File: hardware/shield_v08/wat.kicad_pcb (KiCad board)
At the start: 2 copper layers, 37 parts, among them P101 24VOL, P102 CAUDAL_1, P103 V_IN, P104 PRESION_1, P105 INTENSIDAD_1, P106 18b20, P107 INTENSIDAD_2, P108 15VOL, P109 LCD_I2C, P110 ARD_DI_06, P111 ARD_ALI_04, P112 ARD_AN_04, P113 ARD_I2C_02, U101 ESP-12, U102 Recom-rd, U103 RO-1224S, U104 LM1117, U105 mp-1584

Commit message: [pcb]mejoras version 3
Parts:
- removed P113: ARD_I2C_02, Pin_Headers:Pin_Header_Straight_1x02
- added U106: NANO, oscar_libreria_huellas:arduino_nano, F.Cu at (203.3, 53.2)
- P112: value ARD_AN_04 -> ARD_AN_I2C_06
- moved D104 190.1 mm to (240.0, 27.5)
- moved F101 177.6 mm to (234.5, 24.0), turned to 270 degrees
- moved C109 174.6 mm to (231.7, 62.0), turned to 270 degrees
- moved P110 173.3 mm to (210.9, 45.6), turned to 270 degrees
- moved P103 171.9 mm to (247.0, 20.0), turned to 180 degrees
- moved U101 156.1 mm to (159.1, 32.1), turned to 90 degrees
- moved C108 149.7 mm to (169.0, 38.5)
- moved C105 147.9 mm to (247.5, 33.5)
- moved U105 147.6 mm to (244.0, 49.5), turned to 270 degrees
- moved P101 146.3 mm to (221.0, 95.5), turned to 0 degrees
- moved P108 137.6 mm to (234.0, 95.5), turned to 0 degrees
- moved C106 136.1 mm to (169.0, 45.0), turned to 0 degrees
- moved U103 128.8 mm to (224.5, 80.0), turned to 270 degrees
- moved C107 128.0 mm to (247.5, 64.5), turned to 270 degrees
- moved P102 124.6 mm to (207.5, 19.5), turned to 180 degrees
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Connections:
- P103 pad 1: Net-(F101-Pad1) -> GND
- P103 pad 2: GND -> Net-(F101-Pad1)
- P104 pad 1: GND -> Net-(C103-Pad1)
- P104 pad 2: Net-(C103-Pad1) -> GND
- P105 pad 1: GND -> Net-(C101-Pad1)
- P105 pad 2: Net-(C101-Pad1) -> GND
- P106 pad 1: /Vpc_5V -> GND
- P106 pad 3: GND -> /Vpc_5V
- P107 pad 1: GND -> Net-(C102-Pad1)
- P107 pad 2: Net-(C102-Pad1) -> GND
- P110 pad 3: /e_rx -> /18b20
- P110 pad 4: /e_tx -> /e_rx
- P110 pad 5: /e_rst -> /e_tx
- P110 pad 6: /18b20 -> /e_rst
- P112 pad 5: (no net) -> /sda
- P112 pad 6: (no net) -> /scl

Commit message: [pcb]repongo librerias de huellas
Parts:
- P112: value ARD_AN_I2C_06 -> ARD_AN_I2C
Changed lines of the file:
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@@
       (effects (font (size 1 1) (thickness 0.15)))
     )
-    (fp_text value ARD_AN_I2C_06 (at 0 -3.1 90) (layer F.Fab)
+    (fp_text value ARD_AN_I2C (at 0 -3.1 90) (layer F.Fab)
       (effects (font (size 1 1) (thickness 0.15)))
     )

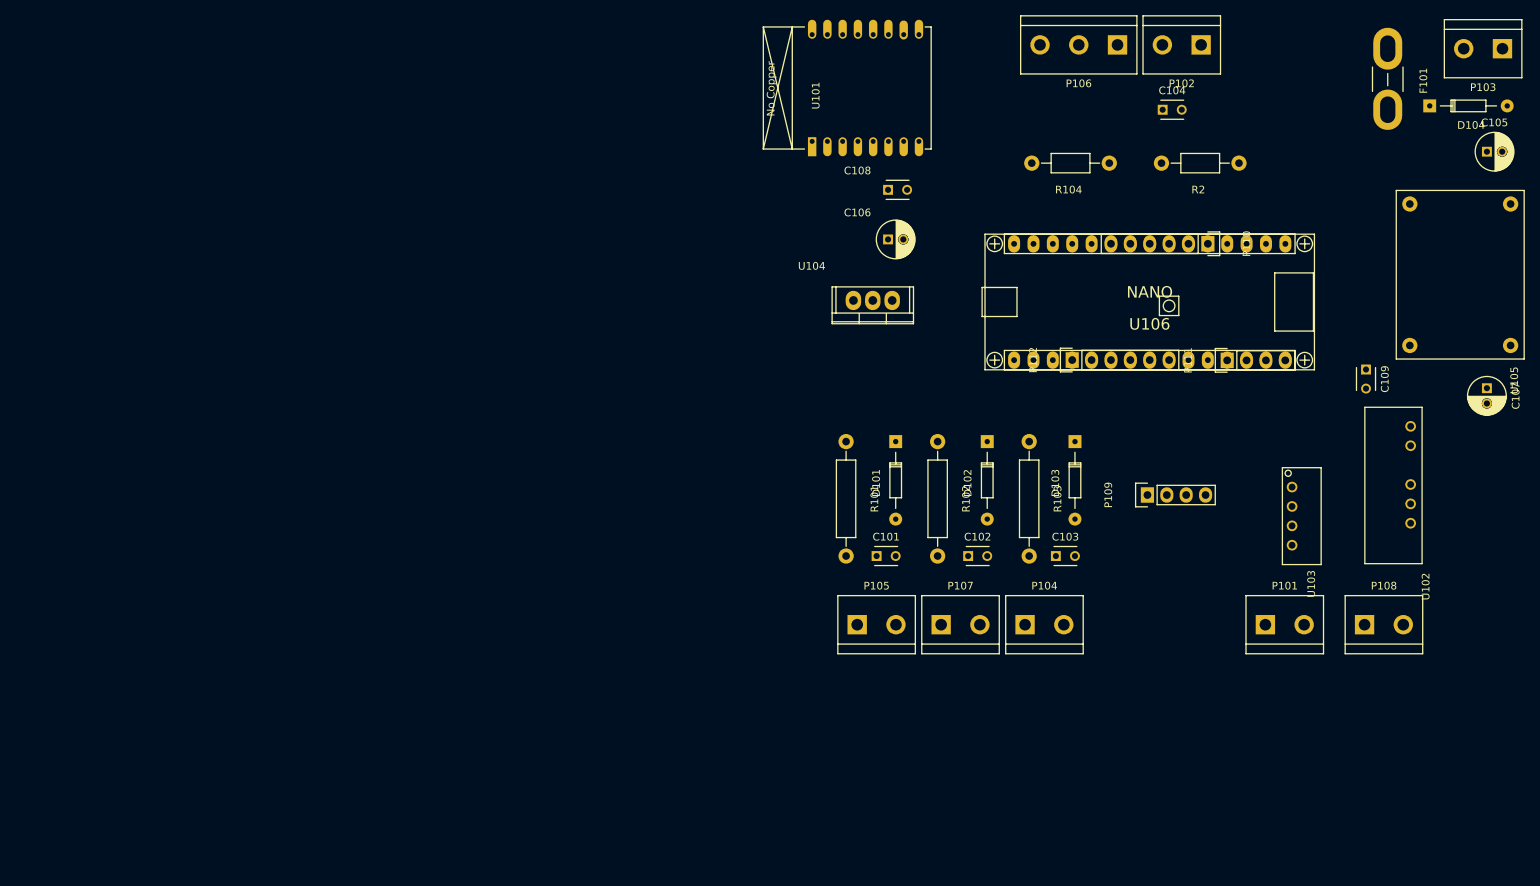
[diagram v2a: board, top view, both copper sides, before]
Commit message: [pdb] cambio posicion nano
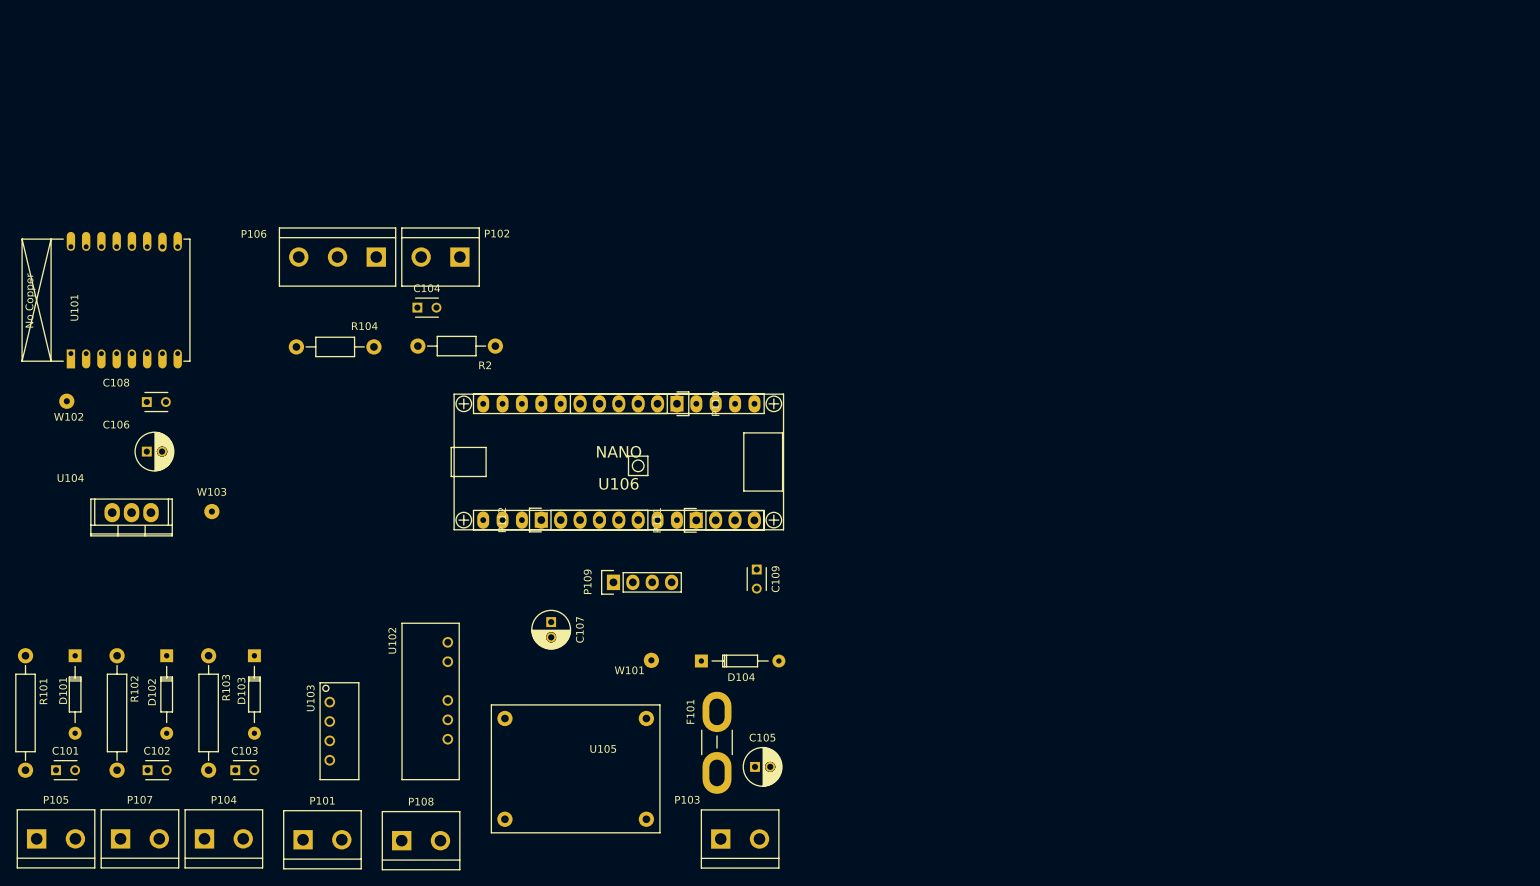
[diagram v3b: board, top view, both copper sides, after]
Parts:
- added W101: +12V, Wire_Pads:SolderWirePad_single_0-8mmDrill, F.Cu at (138.0, 100.2)
- added W102: +3,3V, Wire_Pads:SolderWirePad_single_0-8mmDrill, F.Cu at (61.4, 66.2)
- added W103: +8V, Wire_Pads:SolderWirePad_single_0-8mmDrill, F.Cu at (80.4, 80.7)
- D104: value D -> 1N4007
- moved P103 142.2 mm to (149.6, 123.6), turned to 0 degrees
- moved U105 132.8 mm to (128.2, 114.4), turned to 180 degrees
- moved P108 129.3 mm to (107.8, 123.8)
- moved U102 129.3 mm to (111.3, 97.8)
- moved P101 129.3 mm to (94.9, 123.7)
- moved U103 129.3 mm to (98.4, 108.2)
- moved C107 126.4 mm to (124.8, 95.2)
- moved C105 125.3 mm to (151.6, 114.1)
- moved F101 123.6 mm to (146.6, 110.9), turned to 90 degrees
- moved D104 120.0 mm to (144.5, 100.3)
- moved C101 111.2 mm to (59.9, 114.6)
- moved C102 111.2 mm to (71.9, 114.6)
- moved C103 111.2 mm to (83.4, 114.6)
- moved D101 111.2 mm to (62.4, 99.6)
- moved D102 111.2 mm to (74.4, 99.6)
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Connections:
- net /c_1 renamed /caudal_1
- net /i_1 renamed /intensidad_1
- net /i_2 renamed /intensidad_2
- net /p_1 renamed /presion_1
- P103 pad 1: GND -> Net-(F101-Pad1)
- P103 pad 2: Net-(F101-Pad1) -> GND

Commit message: [pcb]avance version 3
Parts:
- removed U106: NANO, oscar_libreria_huellas:arduino_nano
- added D105: 1N4007, Diodes_ThroughHole:Diode_DO-35_SOD27_Horizontal_RM10, F.Cu at (101.0, 71.0)
- added P113: CONN_02X02, Pin_Headers:Pin_Header_Straight_2x02, F.Cu at (145.6, 90.0)
- moved P103 75.2 mm to (147.8, 48.4), turned to 180 degrees
- moved F101 59.7 mm to (136.1, 52.2), turned to 270 degrees
- moved D104 43.3 mm to (142.0, 57.0)
- moved C107 18.9 mm to (106.0, 93.9)
- moved P101 18.1 mm to (112.9, 122.4)
- moved R2 18.0 mm to (100.9, 65.8), turned to 90 degrees
- moved U103 17.0 mm to (115.3, 107.2)
- moved C105 16.4 mm to (148.4, 98.0)
- moved U105 15.3 mm to (143.5, 115.1), turned to 270 degrees
- moved P108 15.1 mm to (122.8, 122.4)
- moved U102 14.9 mm to (126.2, 96.8)
- moved R104 7.30 mm to (95.2, 55.6), turned to 270 degrees
- moved C106 6.23 mm to (77.8, 71.0)
- moved C108 6.23 mm to (78.0, 65.4)
- moved R101 4.53 mm to (59.6, 96.9)
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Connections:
- P103 pad 1: Net-(F101-Pad1) -> GND
- P103 pad 2: GND -> Net-(F101-Pad1)
- P111 pad 1: /Vpc_5V -> Net-(P111-Pad1)
- P111 pad 4: /Var_8V -> Net-(P111-Pad4)
- R2 pad 1: /Vpc_5V -> Net-(D105-Pad1)
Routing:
- net /Vin_12V: track 0.00 -> 121.7 mm
- net /Vpc_5V: track 0.00 -> 112.5 mm, vias 0 -> 2
- net /Var_8V: track 0.00 -> 84.9 mm, vias 0 -> 2
- net /e_rx: track 0.00 -> 76.5 mm
- net /e_tx: track 0.00 -> 75.6 mm
- net /e_rst: track 0.00 -> 69.0 mm
- net /18b20: track 0.00 -> 52.5 mm
- net /caudal_1: track 0.00 -> 50.6 mm
- net /Ves_3V3: track 0.00 -> 43.7 mm
- net Net-(P108-Pad2): track 0.00 -> 21.1 mm
- net Net-(P108-Pad1): track 0.00 -> 17.4 mm
- net Net-(P101-Pad1): track 0.00 -> 11.1 mm
- net Net-(P111-Pad1): track 0.00 -> 9.51 mm
- net Net-(F101-Pad1): track 0.00 -> 9.24 mm
- net Net-(P111-Pad4): track 0.00 -> 8.96 mm
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- added copper zone on B.Cu, net GND
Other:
- board outline added: 101 x 85.1 mm

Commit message: [pcb]version 3 completa
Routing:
- net /Var_8V: track 84.9 -> 174.4 mm
- net /intensidad_1: track 6.11 -> 70.0 mm
- net /intensidad_2: track 5.70 -> 64.5 mm
- net /presion_1: track 6.50 -> 56.7 mm
- net Net-(C102-Pad1): track 3.86 -> 15.1 mm
- net Net-(C101-Pad1): track 3.72 -> 14.8 mm
- net Net-(C103-Pad1): track 4.08 -> 15.1 mm
- net /Vpc_5V: track 112.5 -> 119.1 mm
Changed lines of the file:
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@@
   (general
     (links 77)
-    (no_connects 37)
-    (area 50.114287 36.45 164.050715 136.800001)
+    (no_connects 0)
+    (area 53.724999 42.724999 154.875001 127.975001)
     (thickness 1.6)
     (drawings 24)
-    (tracks 156)
+    (tracks 195)
     (zones 0)
     (modules 41)
@@
     (arrow2b (pts (xy 75.56 58.544) (xy 76.146421 59.670504)))
   )
+  (segment (start 59.6 111.9) (end 59.6 116.4) (width 0.8) (layer B.Cu) (net 1))
+  (segment (start 58.26 117.74) (end 58.26 122.4) (width 0.8) (layer B.Cu) (net 1))
+  (segment (start 59.6 116.4) (end 58.26 117.74) (width 0.8) (layer B.Cu) (net 1))
   (segment (start 59.6 111.9) (end 62.9 111.9) (width 0.8) (layer B.Cu) (net 1))
   (segment (start 62.9 111.9) (end 63.2 111.6) (width 0.8) (layer B.Cu) (net 1))
+  (segment (start 70.15 111.895) (end 70.15 116.05) (width 0.8) (layer B.Cu) (net 3))
+  (segment (start 68.26 117.94) (end 68.26 122.4) (width 0.8) (layer B.Cu) (net 3))
+  (segment (start 70.15 116.05) (end 68.26 117.94) (width 0.8) (layer B.Cu) (net 3))
   (segment (start 70.15 111.895) (end 73.605 111.895) (width 0.8) (layer B.Cu) (net 3))
   (segment (start 73.605 111.895) (end 73.8 111.7) (width 0.8) (layer B.Cu) (net 3))
   (segment (start 68.35 122.31) (end 68.26 122.4) (width 0.8) (layer B.Cu) (net 3))
+  (segment (start 79.8 112) (end 79.8 115.6) (width 0.8) (layer B.Cu) (net 4))
+  (segment (start 78.36 117.04) (end 78.36 122.4) (width 0.8) (layer B.Cu) (net 4))
+  (segment (start 79.8 115.6) (end 78.36 117.04) (width 0.8) (layer B.Cu) (net 4))
   (segment (start 79.8 112) (end 83.6 112) (width 0.8) (layer B.Cu) (net 4))
   (segment (start 83.6 112) (end 83.8 111.8) (width 0.8) (layer B.Cu) (net 4))
@@
   (segment (start 77.19 66.21) (end 78 65.4) (width 1.2) (layer B.Cu) (net 22))
   (segment (start 78 60) (end 78 65.4) (width 1.2) (layer B.Cu) (net 22))
-  (via (at 132 93.9) (size 0.6) (drill 0.4) (layers F.Cu B.Cu) (net 23))
-  (segment (start 136.896 124.498) (end 132.7 120.302) (width 1.2) (layer B.Cu) (net 23))
-  (segment (start 132.7 103.1) (end 132.7 120.302) (width 1.2) (layer B.Cu) (net 23))
-  (segment (start 131.9 102.3) (end 132.7 103.1) (width 1.2) (layer B.Cu) (net 23))
-  (via (at 131.9 102.3) (size 0.6) (drill 0.4) (layers F.Cu B.Cu) (net 23))
-  (segment (start 131.9 94) (end 131.9 102.3) (width 1.2) (layer F.Cu) (net 23))
-  (segment (start 131.9 94) (end 132 93.9) (width 1.2) (layer F.Cu) (net 23))
+  (segment (start 136.896 124.498) (end 136.896 120.296) (width 1.2) (layer B.Cu) (net 23) (status 400000))
+  (segment (start 132.1 93.9) (end 132 93.9) (width 1.2) (layer B.Cu) (net 23))
+  (segment (start 132.2 93.8) (end 132.1 93.9) (width 1.2) (layer B.Cu) (net 23))
+  (via (at 132.2 93.8) (size 1.9) (drill 1) (layers F.Cu B.Cu) (net 23))
+  (segment (start 132.2 104.8) (end 132.2 93.8) (width 1.2) (layer F.Cu) (net 23))
+  (via (at 132.2 104.8) (size 1.9) (drill 1) (layers F.Cu B.Cu) (net 23))
+  (segment (start 132.2 115.6) (end 132.2 104.8) (width 1.2) (layer B.Cu) (net 23))
+  (segment (start 136.896 120.296) (end 132.2 115.6) (width 1.2) (layer B.Cu) (net 23))
+  (segment (start 145.6 92.54) (end 149.56 92.54) (width 0.8) (layer B.Cu) (net 23))
+  (segment (start 149.56 92.54) (end 150.7 91.4) (width 0.8) (layer B.Cu) (net 23))
+  (segment (start 106 93.9) (end 100.3 93.9) (width 1.2) (layer B.Cu) (net 23))
+  (segment (start 72.34 82.26) (end 72.34 78.6) (width 1.2) (layer B.Cu) (net 23))
+  (segment (start 70 84.6) (end 72.34 82.26) (width 1.2) (layer B.Cu) (net 23))
+  (segment (start 63.2 84.6) (end 70 84.6) (width 1.2) (layer B.Cu) (net 23))
+  (segment (start 56.8 91) (end 63.2 84.6) (width 1.2) (layer B.Cu) (net 23))
+  (segment (start 56.8 99.2) (end 56.8 91) (width 1.2) (layer B.Cu) (net 23))
+  (segment (start 58.4 100.8) (end 56.8 99.2) (width 1.2) (layer B.Cu) (net 23))
+  (segment (start 93.4 100.8) (end 58.4 100.8) (width 1.2) (layer B.Cu) (net 23))
+  (segment (start 100.3 93.9) (end 93.4 100.8) (width 1.2) (layer B.Cu) (net 23))
   (segment (start 106 93.9) (end 132 93.9) (width 1.2) (layer B.Cu) (net 23))
   (segment (start 132 93.9) (end 132.9 93.9) (width 1.2) (layer B.Cu) (net 23))
@@
   (segment (start 145.26 48.4) (end 136.3 48.4) (width 1.2) (layer B.Cu) (net 24))
   (segment (start 136.3 48.4) (end 136.1 48.2) (width 1.2) (layer B.Cu) (net 24))
+  (segment (start 88.32 48.4) (end 84 48.4) (width 1.2) (layer B.Cu) (net 25) (status 400000))
+  (segment (start 90.4 72.8) (end 95.2 72.8) (width 1.2) (layer B.Cu) (net 25))
+  (segment (start 84 66.4) (end 90.4 72.8) (width 1.2) (layer B.Cu) (net 25))
+  (segment (start 84 62) (end 84 66.4) (width 1.2) (layer B.Cu) (net 25))
+  (segment (start 83.8 61.8) (end 84 62) (width 1.2) (layer B.Cu) (net 25))
+  (via (at 83.8 61.8) (size 1.9) (drill 1) (layers F.Cu B.Cu) (net 25))
+  (segment (start 83.8 48.2) (end 83.8 61.8) (width 1.2) (layer F.Cu) (net 25))
+  (via (at 83.8 48.2) (size 1.9) (drill 1) (layers F.Cu B.Cu) (net 25))
+  (segment (start 84 48.4) (end 83.8 48.2) (width 1.2) (layer B.Cu) (net 25))
   (segment (start 143.06 92.54) (end 143.06 93.14) (width 1.2) (layer B.Cu) (net 25))
   (segment (start 143.06 93.14) (end 142.4 93.8) (width 1.2) (layer B.Cu) (net 25))
@@
   (segment (start 136 93.8) (end 134.78 92.58) (width 1.2) (layer B.Cu) (net 25))
   (segment (start 134.78 92.58) (end 134.78 90) (width 1.2) (layer B.Cu) (net 25))
-  (segment (start 88.32 48.4) (end 84.4 48.4) (width 1.2) (layer B.Cu) (net 25))
-  (segment (start 88.56 65.76) (end 95.2 65.76) (width 1.2) (layer B.Cu) (net 25))
-  (segment (start 83.8 61) (end 88.56 65.76) (width 1.2) (layer B.Cu) (net 25))
-  (via (at 83.8 61) (size 0.6) (drill 0.4) (layers F.Cu B.Cu) (net 25))
-  (segment (start 83.8 49) (end 83.8 61) (width 1.2) (layer F.Cu) (net 25))
-  (via (at 83.8 49) (size 0.6) (drill 0.4) (layers F.Cu B.Cu) (net 25))
-  (segment (start 84.4 48.4) (end 83.8 49) (width 1.2) (layer B.Cu) (net 25))
-  (segment (start 95.2 65.76) (end 95.2 78.2) (width 1.2) (layer B.Cu) (net 25))
+  (segment (start 95.2 65.76) (end 95.2 72.8) (width 1.2) (layer B.Cu) (net 25))
+  (segment (start 95.2 72.8) (end 95.2 78.2) (width 1.2) (layer B.Cu) (net 25))
   (segment (start 98.16052 81.16052) (end 101.00254 81.16052) (width 1.2) (layer B.Cu) (net 25))
   (segment (start 95.2 78.2) (end 98.16052 81.16052) (width 1.2) (layer B.Cu) (net 25))
@@
   (segment (start 111 58) (end 131 58) (width 0.8) (layer B.Cu) (net 33))
   (segment (start 109.9 56.9) (end 111 58) (width 0.8) (layer B.Cu) (net 33))
+  (segment (start 119.55 81.78) (end 119.55 83.65) (width 0.8) (layer B.Cu) (net 34))
+  (segment (start 65.70754 92.29246) (end 65.70754 96.89552) (width 0.8) (layer B.Cu) (net 34))
+  (segment (start 73.2 84.8) (end 65.70754 92.29246) (width 0.8) (layer B.Cu) (net 34))
+  (segment (start 118.4 84.8) (end 73.2 84.8) (width 0.8) (layer B.Cu) (net 34))
+  (segment (start 119.55 83.65) (end 118.4 84.8) (width 0.8) (layer B.Cu) (net 34))
   (segment (start 59.6 96.9) (end 65.70306 96.9) (width 0.8) (layer B.Cu) (net 34))
   (segment (start 65.70306 96.9) (end 65.70754 96.89552) (width 0.8) (layer B.Cu) (net 34))
+  (segment (start 122.09 81.78) (end 122.09 85.71) (width 0.8) (layer B.Cu) (net 35))
+  (segment (start 75.80254 90.39746) (end 75.80254 97.00052) (width 0.8) (layer B.Cu) (net 35))
+  (segment (start 79 87.2) (end 75.80254 90.39746) (width 0.8) (layer B.Cu) (net 35))
+  (segment (start 120.6 87.2) (end 79 87.2) (width 0.8) (layer B.Cu) (net 35))
+  (segment (start 122.09 85.71) (end 120.6 87.2) (width 0.8) (layer B.Cu) (net 35))
   (segment (start 70.15 96.895) (end 75.69702 96.895) (width 0.8) (layer B.Cu) (net 35))
   (segment (start 75.69702 96.895) (end 75.80254 97.00052) (width 0.8) (layer B.Cu) (net 35))
+  (segment (start 124.63 81.78) (end 124.63 86.97) (width 0.8) (layer B.Cu) (net 36))
+  (segment (start 86.30254 92.69746) (end 86.30254 97.00052) (width 0.8) (layer B.Cu) (net 36))
+  (segment (start 89.4 89.6) (end 86.30254 92.69746) (width 0.8) (layer B.Cu) (net 36))
+  (segment (start 122 89.6) (end 89.4 89.6) (width 0.8) (layer B.Cu) (net 36))
+  (segment (start 124.63 86.97) (end 122 89.6) (width 0.8) (layer B.Cu) (net 36))
   (segment (start 79.8 97) (end 86.30202 97) (width 0.8) (layer B.Cu) (net 36))
   (segment (start 86.30202 97) (end 86.30254 97.00052) (width 0.8) (layer B.Cu) (net 36))
@@
     (connect_pads (clearance 0.508))
     (min_thickness 0.254)
-    (fill (arc_segments 16) (thermal_gap 0.508) (thermal_bridge_width 0.508))
+    (fill yes (arc_segments 16) (thermal_gap 0.508) (thermal_bridge_width 0.508))
     (polygon
       (pts
